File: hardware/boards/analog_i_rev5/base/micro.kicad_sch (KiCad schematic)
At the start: 81 parts, among them IC1 STM32H743ZIT6, J4 Conn_02x07_Odd_Even, Y1 SiT1602BI-21-33S-48.000000

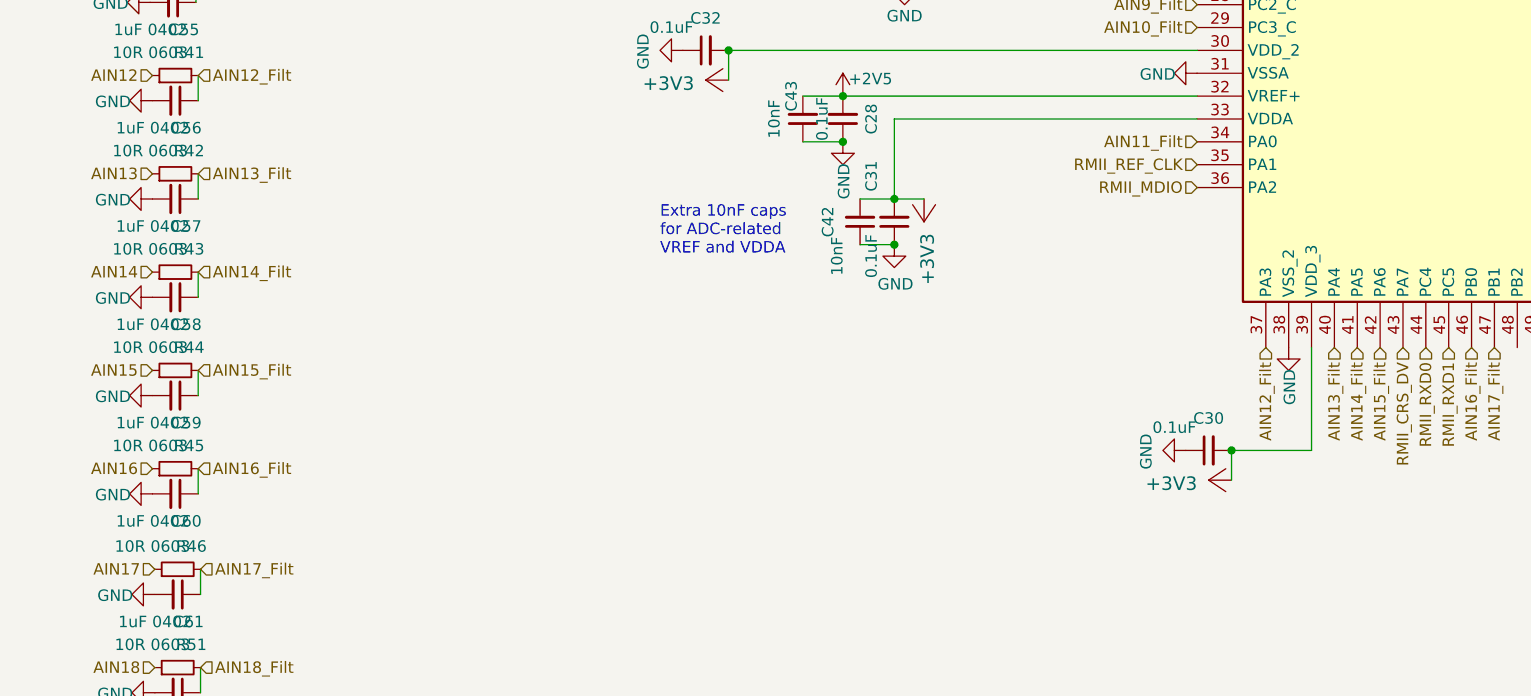
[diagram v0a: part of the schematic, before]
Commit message: limit amp voltage outputs to 3.3V
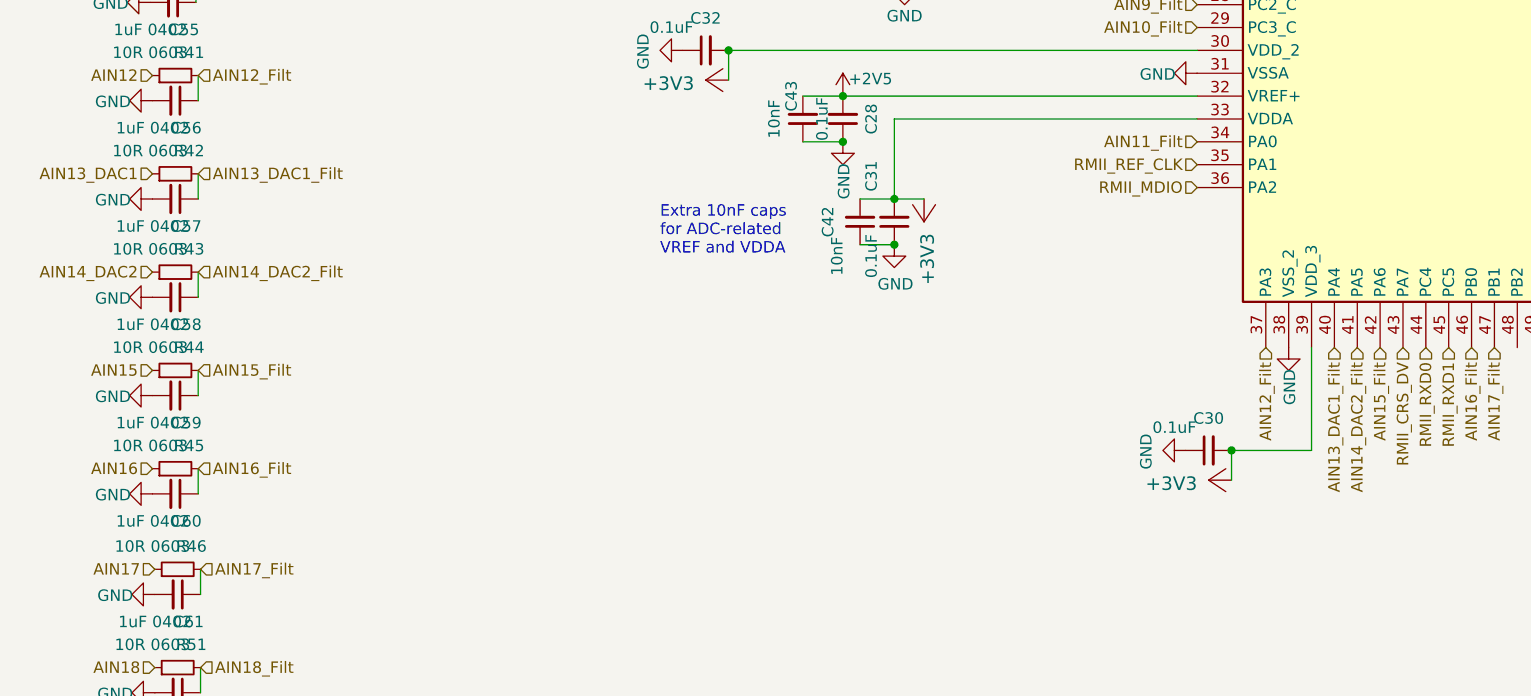
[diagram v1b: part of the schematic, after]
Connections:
- net AIN13 renamed AIN13_DAC1
- net AIN13_Filt renamed AIN13_DAC1_Filt
- net AIN14 renamed AIN14_DAC2
- net AIN14_Filt renamed AIN14_DAC2_Filt
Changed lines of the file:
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@@
 		)
 	)
-	(hierarchical_label "AIN14_Filt"
+	(hierarchical_label "AIN14_DAC2_Filt"
 		(shape input)
 		(at 171.196 235.966 270)
@@
 		)
 	)
-	(hierarchical_label "AIN14_Filt"
+	(hierarchical_label "AIN14_DAC2_Filt"
 		(shape input)
 		(at 42.418 227.584 0)
@@
 		)
 	)
-	(hierarchical_label "AIN13_Filt"
+	(hierarchical_label "AIN13_DAC1_Filt"
 		(shape input)
 		(at 168.656 235.966 270)
@@
 		)
 	)
-	(hierarchical_label "AIN13"
+	(hierarchical_label "AIN13_DAC1"
 		(shape input)
 		(at 37.338 216.662 180)
@@
 		)
 	)
-	(hierarchical_label "AIN13_Filt"
+	(hierarchical_label "AIN13_DAC1_Filt"
 		(shape input)
 		(at 42.418 216.662 0)
@@
 		)
 	)
-	(hierarchical_label "AIN14"
+	(hierarchical_label "AIN14_DAC2"
 		(shape input)
 		(at 37.338 227.584 180)

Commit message: update base layout
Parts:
- removed C57, C58: 1uF 0402, Capacitor_SMD:C_0402_1005Metric, symbol Device:C_Small
- removed R42, R43: 10R 0603, Resistor_SMD:R_0603_1608Metric, symbol Device:R_Small
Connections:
- net AIN13_DAC1_Filt renamed AIN13_DAC0
- net AIN14_DAC2_Filt renamed AIN14_DAC1
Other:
- note added: "TIM4_CH1 and _CH2 are both needed in order to capture both frequency and pulse width for PWM input, because one channel can't map to multiple compare-and-capture modules. Neither frequency input has pulse width info because configuring the registers to extract pulse width causes failures in other timers."
- note removed: "TIM4_CH1 and _CH2 are both needed in order to capture both frequency and pulse width for PWM input, because one channel can't map to multiple compare-and-capture modules. No other timer module that might be used as a frequency input has a second channel pin available, so only one frequency input has pulse width info."
